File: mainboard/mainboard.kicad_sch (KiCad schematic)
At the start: 47 parts, among them J1 Servo, J2 ADC Pins, J3 USB Data, J4 Button Interface, J5 Power, J6 Release Button, J8 GPIO Pins, Q1 BSS138, SW1 SW_Push, U1 RP2040, U2 W25Q128JVS, U3 RV-3028-C7, U4 ITR9608-F, Y1 Crystal_ABM8

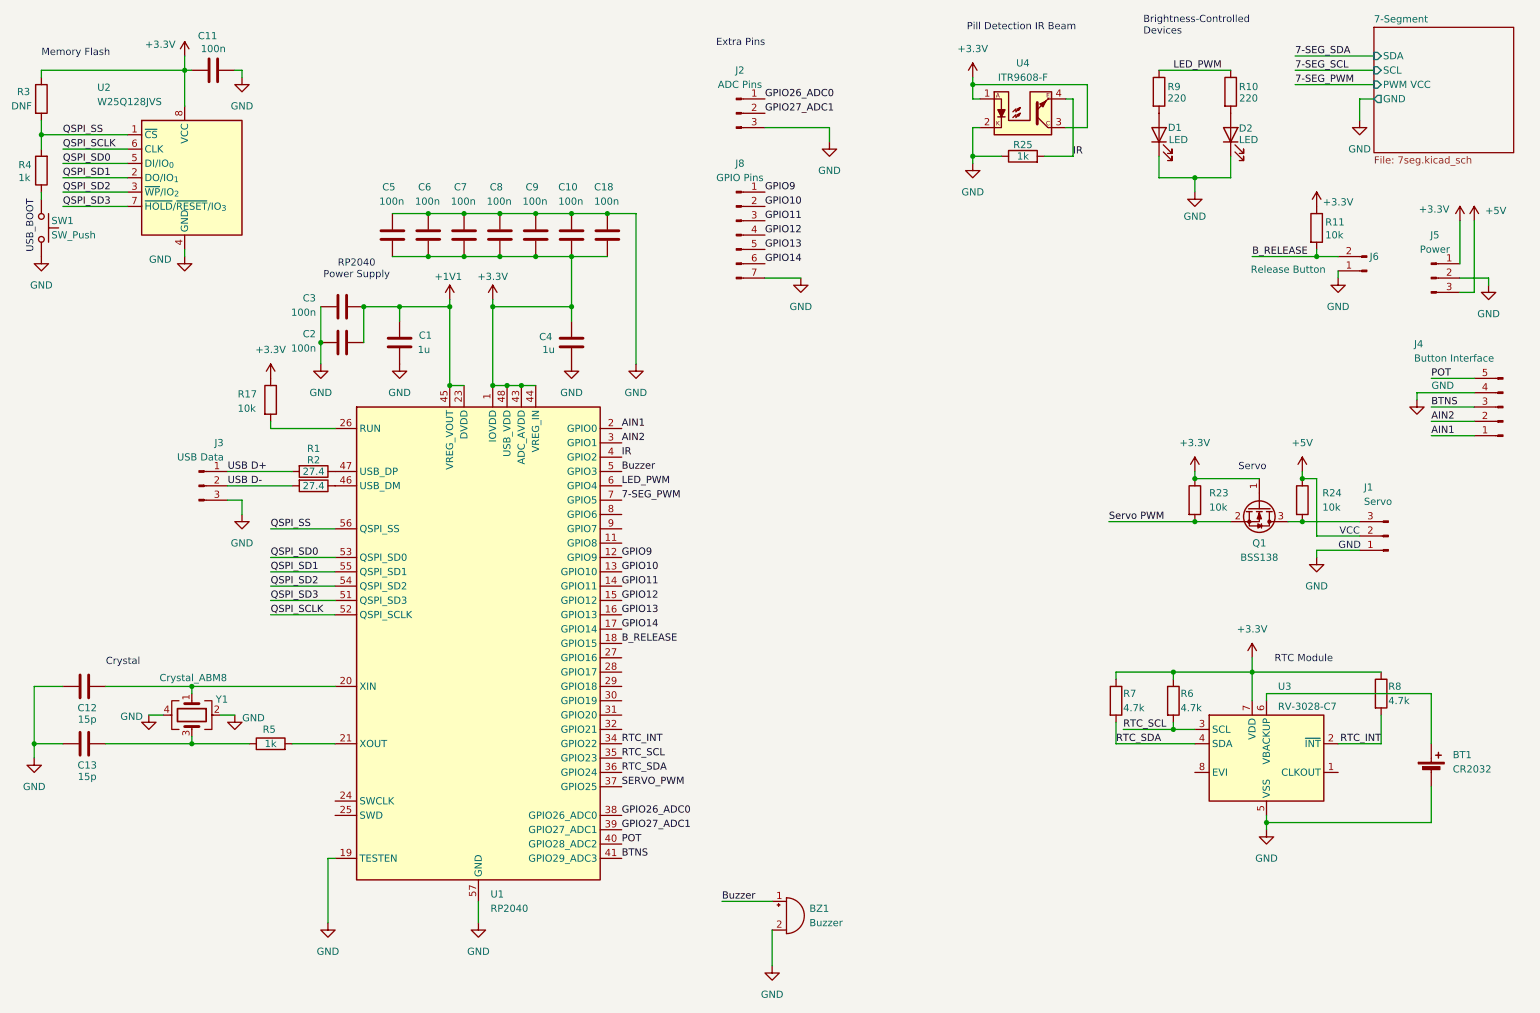
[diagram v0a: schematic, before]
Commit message: updated all ground pin connectors to pin 1
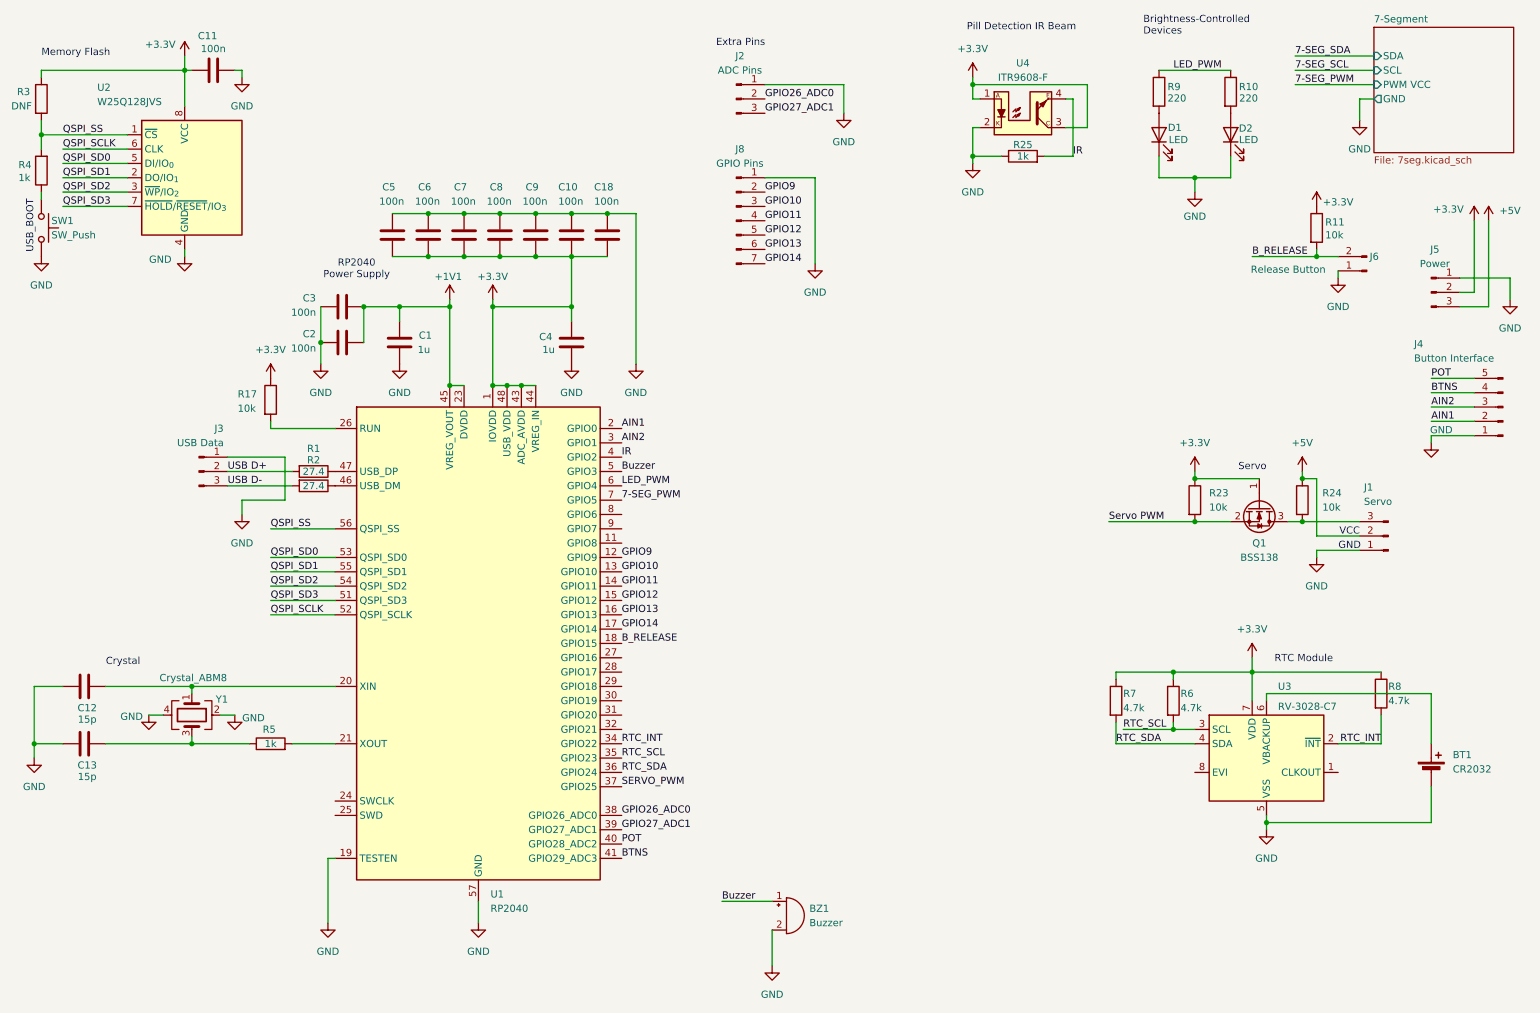
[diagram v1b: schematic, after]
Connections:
- net +3.3V: now also J5.2 (Pin_2); no longer J5.1 (Pin_1)
- net AIN1: now also J4.2 (Pin_2); no longer J4.1 (Pin_1)
- net AIN2: now also J4.3 (Pin_3); no longer J4.2 (Pin_2)
- net BTNS: now also J4.4 (Pin_4); no longer J4.3 (Pin_3)
- net GND: now also J2.1 (Pin_1), J3.1 (Pin_1), J4.1 (Pin_1), J5.1 (Pin_1), J8.1 (Pin_1); no longer J2.3 (Pin_3), J3.3 (Pin_3), J4.4 (Pin_4), J5.2 (Pin_2), J8.7 (Pin_7)
- net GPIO10: now also J8.3 (Pin_3); no longer J8.2 (Pin_2)
- net GPIO11: now also J8.4 (Pin_4); no longer J8.3 (Pin_3)
- net GPIO12: now also J8.5 (Pin_5); no longer J8.4 (Pin_4)
- net GPIO13: now also J8.6 (Pin_6); no longer J8.5 (Pin_5)
- net GPIO14: now also J8.7 (Pin_7); no longer J8.6 (Pin_6)
- net GPIO26_ADC0: now also J2.2 (Pin_2); no longer J2.1 (Pin_1)
- net GPIO27_ADC1: now also J2.3 (Pin_3); no longer J2.2 (Pin_2)
- net GPIO9: now also J8.2 (Pin_2); no longer J8.1 (Pin_1)
- net USB D+: now also J3.2 (Pin_2); no longer J3.1 (Pin_1)
- net USB D-: now also J3.3 (Pin_3); no longer J3.2 (Pin_2)
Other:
- moved on the sheet: J2, J3, J5, J8

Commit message: reorganized resistor numbers
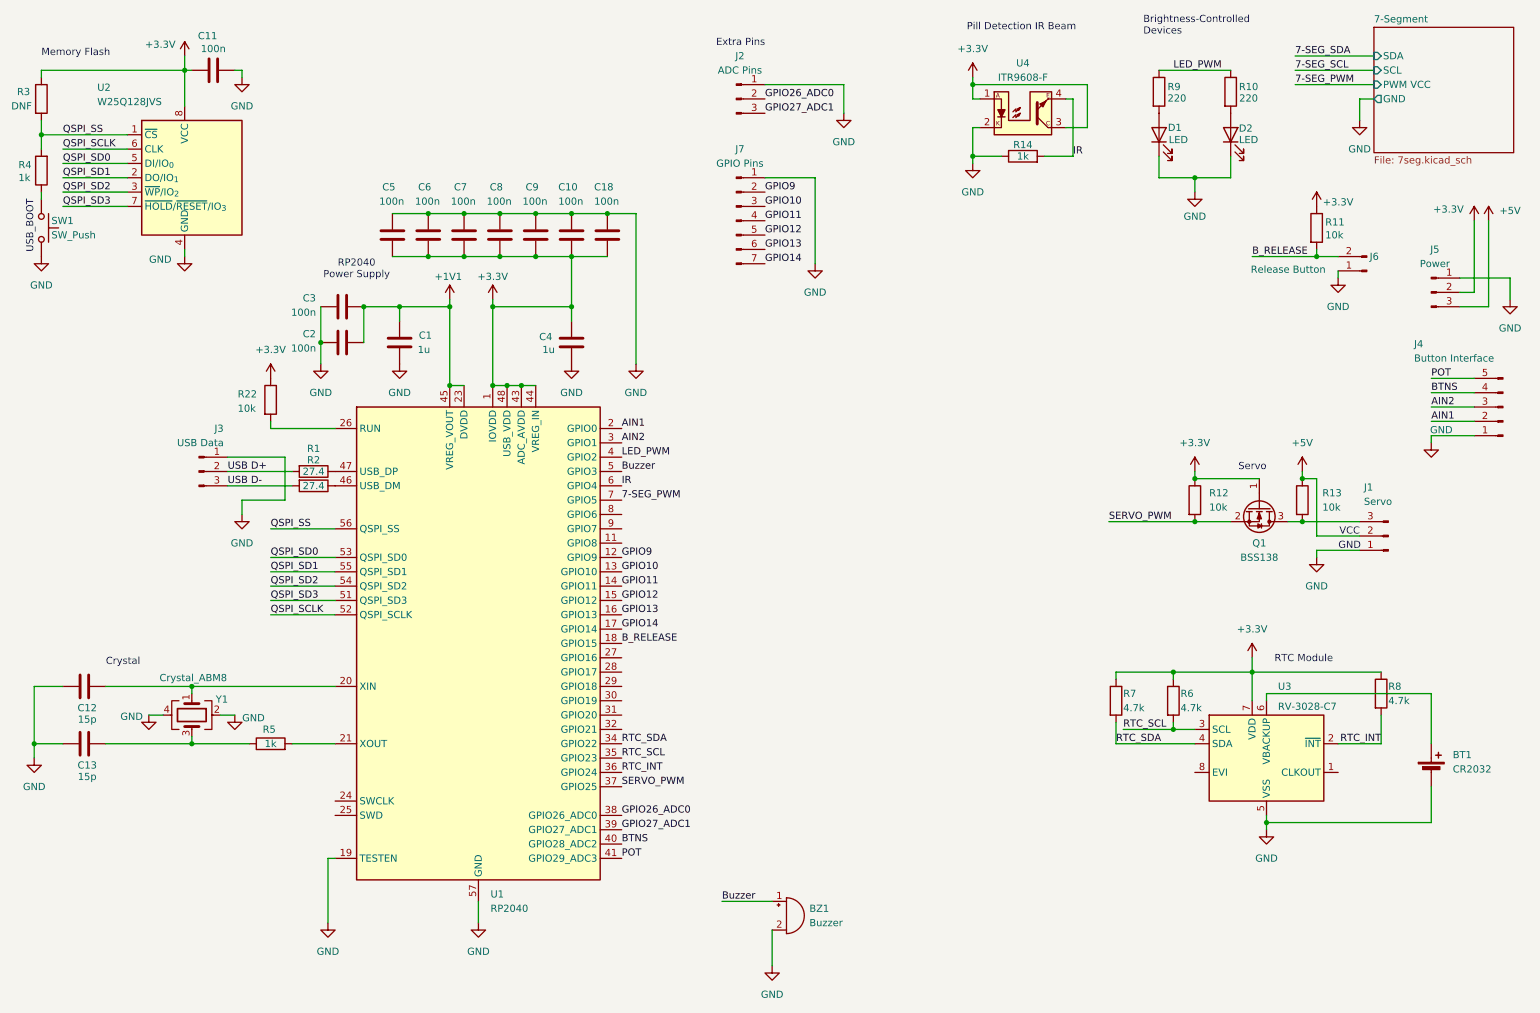
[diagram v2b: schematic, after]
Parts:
- J6: footprint (none) -> Connector_JST:JST_EH_B2B-EH-A_1x02_P2.50mm_Vertical
- R14: renamed from R25; footprint (none) -> Resistor_SMD:R_0603_1608Metric
- U4: footprint OptoDevice:Everlight_ITR9608-F -> OptoDevice:PIRUPT_14mm
- renumbered J8 to J7, R23 to R12, R24 to R13, R17 to R22
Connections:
- net Servo PWM is gone; now on net SERVO_PWM: Q1.2 (S), R12.2
- net BTNS: now also U1.40 (GPIO28_ADC2); no longer U1.41 (GPIO29_ADC3)
- net IR: now also U1.6 (GPIO4); no longer U1.4 (GPIO2)
- net LED_PWM: now also U1.4 (GPIO2); no longer U1.6 (GPIO4)
- net POT: now also U1.41 (GPIO29_ADC3); no longer U1.40 (GPIO28_ADC2)
- net RTC_INT: now also U1.36 (GPIO24); no longer U1.34 (GPIO22)
- net RTC_SDA: now also U1.34 (GPIO22); no longer U1.36 (GPIO24)
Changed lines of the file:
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@@
 	)
 	(label "POT"
-		(at 124.46 161.29 0)
+		(at 124.46 163.83 0)
 		(effects
 			(font
@@
 		)
 	)
-	(label "Servo PWM"
+	(label "SERVO_PWM"
 		(at 210.82 104.14 0)
 		(effects
@@
 	)
 	(label "LED_PWM"
-		(at 124.46 97.79 0)
+		(at 124.46 92.71 0)
 		(effects
 			(font
@@
 	)
 	(label "BTNS"
-		(at 124.46 163.83 0)
+		(at 124.46 161.29 0)
 		(effects
 			(font
@@
 	)
 	(label "IR"
-		(at 124.46 92.71 0)
+		(at 124.46 97.79 0)
 		(effects
 			(font
@@
 	)
 	(label "RTC_SDA"
-		(at 124.46 148.59 0)
+		(at 124.46 143.51 0)
 		(effects
 			(font
@@
 	)
 	(label "RTC_INT"
-		(at 124.46 143.51 0)
+		(at 124.46 148.59 0)
 		(effects
 			(font
@@
 			)
 		)
-		(property "Footprint" "OptoDevice:Everlight_ITR9608-F"
+		(property "Footprint" "OptoDevice:PIRUPT_14mm"
 			(at 195.58 38.1 0)
 			(effects
@@
 		(dnp no)
 		(fields_autoplaced yes)
-		(property "Reference" "R23"
+		(property "Reference" "R12"
 			(at 228.6 99.0599 0)
 			(effects
@@
 			(project ""
 				(path "/57f2b6ac-3611-4b16-b8a1-8e91b00e0208"
-					(reference "R23")
+					(reference "R12")
 					(unit 1)
 				)
@@
 		(on_board yes)
 		(dnp no)
-		(property "Reference" "R25"
+		(property "Reference" "R14"
 			(at 195.58 37.338 90)
 			(effects
@@
 			)
 		)
-		(property "Footprint" ""
+		(property "Footprint" "Resistor_SMD:R_0603_1608Metric"
 			(at 195.58 41.148 90)
 			(effects
@@
 			(project ""
 				(path "/57f2b6ac-3611-4b16-b8a1-8e91b00e0208"
-					(reference "R25")
+					(reference "R14")
 					(unit 1)
 				)
@@
 		(on_board yes)
 		(dnp no)
-		(property "Reference" "R24"
+		(property "Reference" "R13"
 			(at 248.666 99.06 0)
 			(effects
@@
 			(project "pill_dispenser"
 				(path "/57f2b6ac-3611-4b16-b8a1-8e91b00e0208"
-					(reference "R24")
+					(reference "R13")
 					(unit 1)
 				)
@@
 		(dnp no)
 		(fields_autoplaced yes)
-		(property "Reference" "J8"
+		(property "Reference" "J7"
 			(at 145.415 38.1 0)
 			(effects
@@
 			(project ""
 				(path "/57f2b6ac-3611-4b16-b8a1-8e91b00e0208"
-					(reference "J8")
+					(reference "J7")
 					(unit 1)
 				)
@@
 		(on_board yes)
 		(dnp no)
-		(property "Reference" "R17"
+		(property "Reference" "R22"
 			(at 56.388 81.534 0)
 			(effects
@@
 			(project ""
 				(path "/57f2b6ac-3611-4b16-b8a1-8e91b00e0208"
-					(reference "R17")
+					(reference "R22")
 					(unit 1)
 				)
@@
 			)
 		)
-		(property "Footprint" ""
+		(property "Footprint" "Connector_JST:JST_EH_B2B-EH-A_1x02_P2.50mm_Vertical"
 			(at 256.54 59.69 0)
 			(effects

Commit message: added test points
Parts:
- added TP1: GND, TestPoint:TestPoint_Pad_4.0x4.0mm, symbol Connector:TestPoint
- added TP2: 5V, TestPoint:TestPoint_Pad_D2.0mm, symbol Connector:TestPoint
- added TP3: 3V3, TestPoint:TestPoint_Pad_D2.0mm, symbol Connector:TestPoint
- added TP4: 1V1, TestPoint:TestPoint_Pad_D1.5mm, symbol Connector:TestPoint
- added TP5: Pot, TestPoint:TestPoint_Pad_D1.5mm, symbol Connector:TestPoint
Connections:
- net +1V1: now also TP4.1
- net +3.3V: now also TP3.1
- net +5V: now also TP2.1
- net GND: now also TP1.1
- net POT: now also TP5.1
